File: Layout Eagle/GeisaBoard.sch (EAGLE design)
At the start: 20 parts, among them IC1 4052N, IC2 4052N, U1 328P

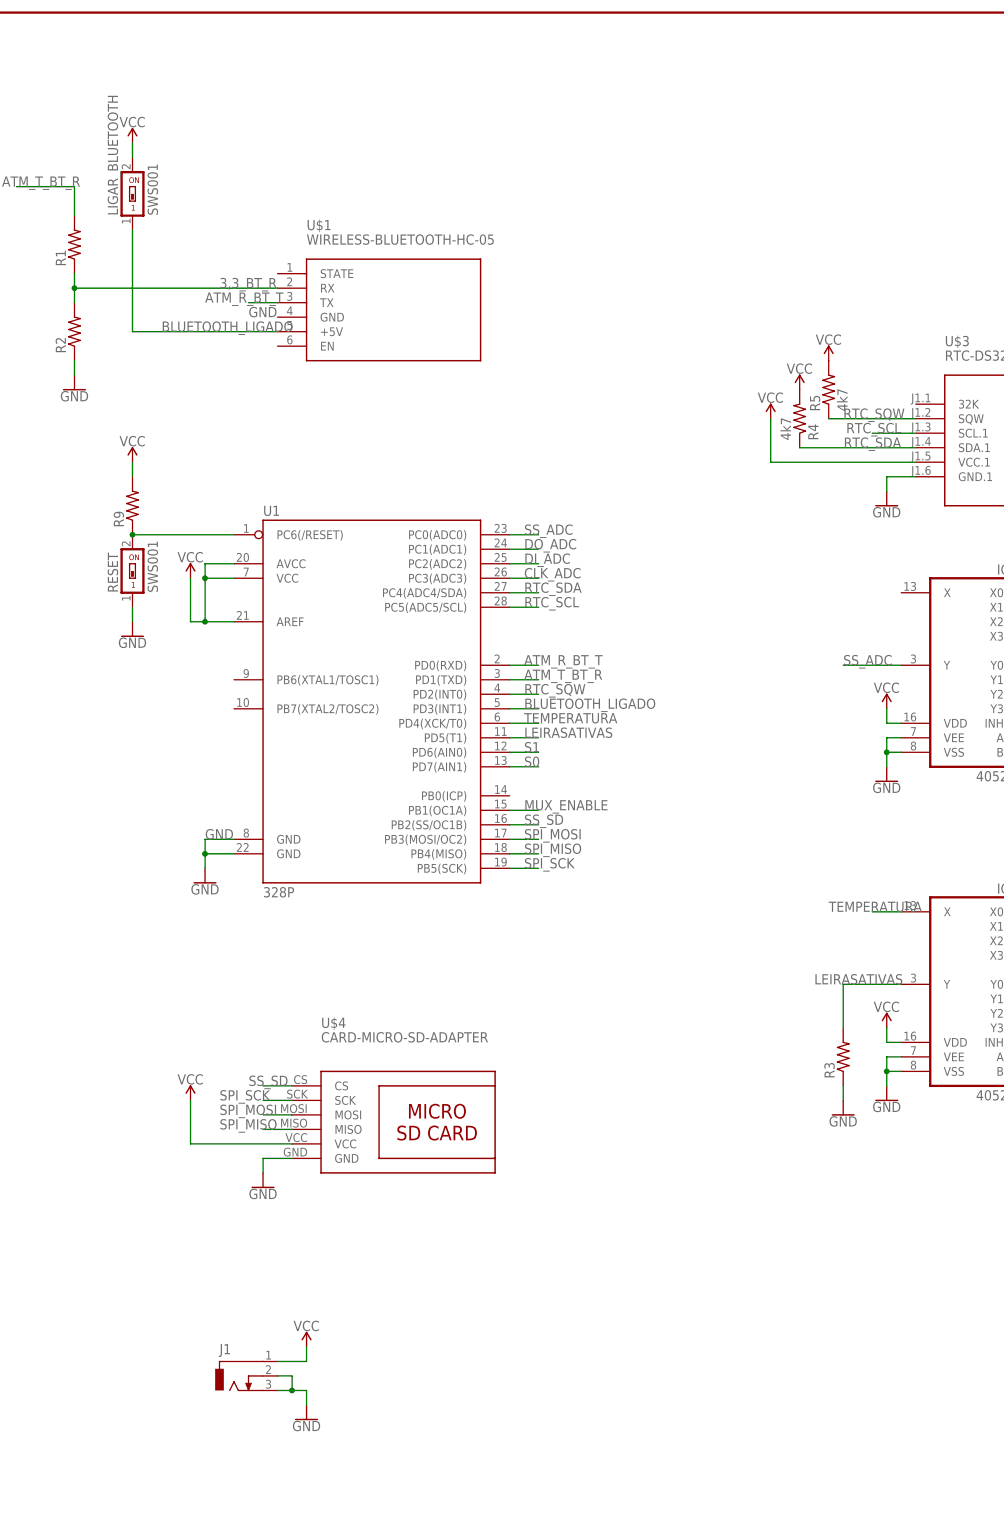
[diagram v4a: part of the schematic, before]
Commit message: Novo layout feito com melhores definições de espessura de trilhas e outros parâmetros
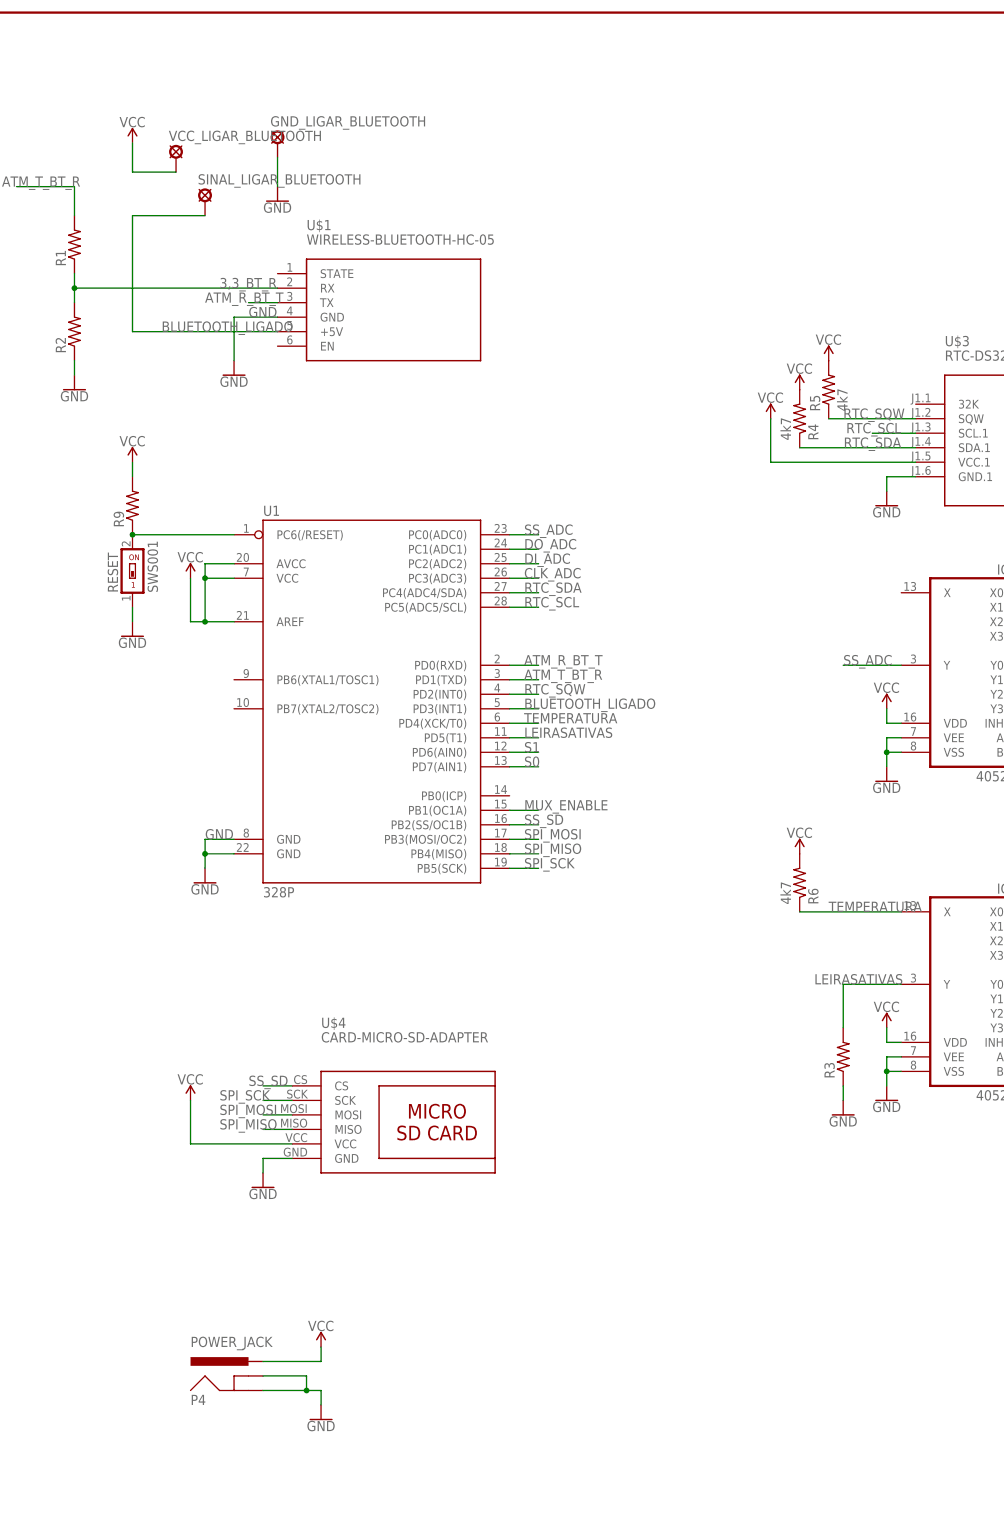
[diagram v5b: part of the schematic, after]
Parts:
- removed J1: (no value), con-jack:DCJ0303
- removed LIGAR_BLUETOOTH: SWS001, smd-special:SWS001
- added GND_LIGAR_BLUETOOTH, SINAL_LIGAR_BLUETOOTH, VCC_LIGAR_BLUETOOTH: LSP11, solpad:LSP11
- added P4: POWER_JACK, SparkFun-Connectors:POWER_JACK
- added R6: 4k7, rcl:R-US_0204/7
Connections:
- net BLUETOOTH_LIGADO: now also SINAL_LIGAR_BLUETOOTH.MP; no longer LIGAR_BLUETOOTH.1
- net GND: now also GND_LIGAR_BLUETOOTH.MP, P4.GND, P4.GNDBREAK, U$1.GND; no longer J1.2, J1.3
- net TEMPERATURA: now also R6.1
- net VCC: now also P4.PWR, R6.2, VCC_LIGAR_BLUETOOTH.MP; no longer J1.1, LIGAR_BLUETOOTH.2
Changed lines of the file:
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@@
 <?xml version="1.0" encoding="utf-8"?>
 <!DOCTYPE eagle SYSTEM "eagle.dtd">
-<eagle version="8.7.0">
+<eagle version="8.3.2">
 <drawing>
 <settings>
@@
 </variantdefs>
 <classes>
-<class number="0" name="default" width="0" drill="0">
+<class number="0" name="default" width="0.508" drill="0">
+</class>
+<class number="1" name="alimentação" width="1.016" drill="0">
 </class>
 </classes>
@@
 <part name="R9" library="rcl" library_urn="urn:adsk.eagle:library:334" deviceset="R-US_" device="0204/7" package3d_urn="urn:adsk.eagle:package:23498/1"/>
 <part name="RESET" library="smd-special" library_urn="urn:adsk.eagle:library:362" deviceset="SWS001" device="" package3d_urn="urn:adsk.eagle:package:26467/1"/>
-<part name="LIGAR_BLUETOOTH" library="smd-special" library_urn="urn:adsk.eagle:library:362" deviceset="SWS001" device="" package3d_urn="urn:adsk.eagle:package:26467/1"/>
 <part name="GND6" library="SparkFun-PowerSymbols" deviceset="GND" device=""/>
 <part name="GND7" library="SparkFun-PowerSymbols" deviceset="GND" device=""/>
@@
 <part name="SUPPLY8" library="SparkFun-PowerSymbols" deviceset="VCC" device=""/>
 <part name="SUPPLY9" library="SparkFun-PowerSymbols" deviceset="VCC" device=""/>
-<part name="J1" library="con-jack" library_urn="urn:adsk.eagle:library:154" deviceset="DCJ0303" device="" package3d_urn="urn:adsk.eagle:package:7493/1"/>
 <part name="GND11" library="SparkFun-PowerSymbols" deviceset="GND" device=""/>
 <part name="GND12" library="SparkFun-PowerSymbols" deviceset="GND" device=""/>
@@
 <part name="U$3" library="Geisa" deviceset="RTC-DS3231-AT24C32" device=""/>
 <part name="U$4" library="Geisa" deviceset="CARD-MICRO-SD-ADAPTER" device=""/>
+<part name="GND5" library="SparkFun-PowerSymbols" deviceset="GND" device=""/>
+<part name="R6" library="rcl" library_urn="urn:adsk.eagle:library:334" deviceset="R-US_" device="0204/7" package3d_urn="urn:adsk.eagle:package:23498/1" value="4k7"/>
+<part name="SUPPLY11" library="SparkFun-PowerSymbols" deviceset="VCC" device=""/>
+<part name="VCC_LIGAR_BLUETOOTH" library="solpad" library_urn="urn:adsk.eagle:library:364" deviceset="LSP11" device="" package3d_urn="urn:adsk.eagle:package:26502/1"/>
+<part name="SINAL_LIGAR_BLUETOOTH" library="solpad" library_urn="urn:adsk.eagle:library:364" deviceset="LSP11" device="" package3d_urn="urn:adsk.eagle:package:26502/1"/>
+<part name="GND_LIGAR_BLUETOOTH" library="solpad" library_urn="urn:adsk.eagle:library:364" deviceset="LSP11" device="" package3d_urn="urn:adsk.eagle:package:26502/1"/>
+<part name="GND10" library="SparkFun-PowerSymbols" deviceset="GND" device=""/>
+<part name="P4" library="SparkFun-Connectors" deviceset="POWER_JACK" device=""/>
 </parts>
 <sheets>
@@
 <instance part="R9" gate="G$1" x="-109.22" y="53.34" rot="R90"/>
 <instance part="RESET" gate="G$1" x="-109.22" y="40.64"/>
-<instance part="LIGAR_BLUETOOTH" gate="G$1" x="-109.22" y="106.68"/>
 <instance part="GND6" gate="1" x="149.86" y="81.28" rot="MR0"/>
 <instance part="GND7" gate="1" x="149.86" y="43.18" rot="MR0"/>
@@
 <instance part="SUPPLY8" gate="G$1" x="124.46" y="60.96"/>
 <instance part="SUPPLY9" gate="G$1" x="124.46" y="99.06"/>
-<instance part="J1" gate="G$1" x="-91.44" y="-99.06"/>
 <instance part="GND11" gate="1" x="15.24" y="-53.34"/>
 <instance part="GND12" gate="1" x="-86.36" y="-66.04"/>
@@
 <instance part="GND15" gate="1" x="-119.38" y="73.66"/>
 <instance part="GND16" gate="1" x="22.86" y="53.34"/>
-<instance part="GND17" gate="1" x="-78.74" y="-106.68"/>
+<instance part="GND17" gate="1" x="-76.2" y="-106.68"/>
 <instance part="SUPPLY4" gate="G$1" x="2.54" y="68.58"/>
 <instance part="SUPPLY5" gate="G$1" x="-99.06" y="-50.8"/>
@@
 <instance part="SUPPLY13" gate="G$1" x="-109.22" y="60.96"/>
 <instance part="SUPPLY14" gate="G$1" x="-109.22" y="116.84"/>
-<instance part="SUPPLY15" gate="G$1" x="-78.74" y="-93.98"/>
+<instance part="SUPPLY15" gate="G$1" x="-76.2" y="-93.98"/>
 <instance part="R4" gate="G$1" x="7.62" y="68.58" rot="MR90"/>
 <instance part="R5" gate="G$1" x="12.7" y="73.66" rot="R90"/>
@@
 <instance part="U$3" gate="G$1" x="45.72" y="66.04"/>
 <instance part="U$4" gate="G$1" x="-58.42" y="-58.42"/>
+<instance part="GND5" gate="1" x="-91.44" y="76.2"/>
+<instance part="R6" gate="G$1" x="7.62" y="-12.7" rot="MR90"/>
+<instance part="SUPPLY11" gate="G$1" x="7.62" y="-7.62" rot="MR0"/>
+<instance part="VCC_LIGAR_BLUETOOTH" gate="1" x="-101.6" y="114.3"/>
+<instance part="SINAL_LIGAR_BLUETOOTH" gate="1" x="-96.52" y="106.68"/>
+<instance part="GND_LIGAR_BLUETOOTH" gate="1" x="-83.82" y="116.84"/>
+<instance part="GND10" gate="1" x="-83.82" y="106.68"/>
+<instance part="P4" gate="G$1" x="-88.9" y="-104.14"/>
 </instances>
 <busses>
@@
 </segment>
 </net>
-<net name="GND" class="0">
+<net name="GND" class="1">
 <segment>
 <wire x1="-96.52" y1="-10.16" x2="-96.52" y2="-7.62" width="0.1524" layer="91"/>
@@
 </segment>
 <segment>
-<pinref part="J1" gate="G$1" pin="3"/>
 <pinref part="GND17" gate="1" pin="GND"/>
-<wire x1="-83.82" y1="-101.6" x2="-81.28" y2="-101.6" width="0.1524" layer="91"/>
-<wire x1="-81.28" y1="-101.6" x2="-78.74" y2="-101.6" width="0.1524" layer="91"/>
-<wire x1="-78.74" y1="-101.6" x2="-78.74" y2="-104.14" width="0.1524" layer="91"/>
-<pinref part="J1" gate="G$1" pin="2"/>
-<wire x1="-83.82" y1="-99.06" x2="-81.28" y2="-99.06" width="0.1524" layer="91"/>
-<wire x1="-81.28" y1="-99.06" x2="-81.28" y2="-101.6" width="0.1524" layer="91"/>
-<junction x="-81.28" y="-101.6"/>
+<wire x1="-86.36" y1="-101.6" x2="-78.74" y2="-101.6" width="0.1524" layer="91"/>
+<wire x1="-78.74" y1="-101.6" x2="-76.2" y2="-101.6" width="0.1524" layer="91"/>
+<wire x1="-76.2" y1="-101.6" x2="-76.2" y2="-104.14" width="0.1524" layer="91"/>
+<wire x1="-86.36" y1="-99.06" x2="-78.74" y2="-99.06" width="0.1524" layer="91"/>
+<wire x1="-78.74" y1="-99.06" x2="-78.74" y2="-101.6" width="0.1524" layer="91"/>
+<junction x="-78.74" y="-101.6"/>
+<pinref part="P4" gate="G$1" pin="GND"/>
+<pinref part="P4" gate="G$1" pin="GNDBREAK"/>
 </segment>
 <segment>
@@
 <wire x1="22.86" y1="58.42" x2="22.86" y2="55.88" width="0.1524" layer="91"/>
 </segment>
+<segment>
+<pinref part="GND10" gate="1" pin="GND"/>
+<pinref part="GND_LIGAR_BLUETOOTH" gate="1" pin="MP"/>
+<wire x1="-83.82" y1="109.22" x2="-83.82" y2="114.3" width="0.1524" layer="91"/>
+</segment>
+<segment>
+<pinref part="U$1" gate="G$1" pin="GND"/>
+<pinref part="GND5" gate="1" pin="GND"/>
+<wire x1="-83.82" y1="86.36" x2="-91.44" y2="86.36" width="0.1524" layer="91"/>
+<wire x1="-91.44" y1="86.36" x2="-91.44" y2="78.74" width="0.1524" layer="91"/>
+</segment>
 </net>
 <net name="N$12" class="0">
@@
 <net name="TEMPERATURA" class="0">
 <segment>
-<wire x1="25.4" y1="-17.78" x2="20.32" y2="-17.78" width="0.1524" layer="91"/>
 <label x="12.7" y="-17.78" size="1.778" layer="95"/>
 <pinref part="IC2" gate="A" pin="X"/>
+<pinref part="R6" gate="G$1" pin="1"/>
+<wire x1="25.4" y1="-17.78" x2="7.62" y2="-17.78" width="0.1524" layer="91"/>
 </segment>
 <segment>
@@
 </segment>
 </net>
-<net name="VCC" class="0">
+<net name="VCC" class="1">
 <segment>
 <wire x1="124.46" y1="-25.4" x2="129.54" y2="-25.4" width="0.1524" layer="91"/>
@@
 </segment>
 <segment>
-<pinref part="J1" gate="G$1" pin="1"/>
 <pinref part="SUPPLY15" gate="G$1" pin="VCC"/>
-<wire x1="-83.82" y1="-96.52" x2="-78.74" y2="-96.52" width="0.1524" layer="91"/>
-<wire x1="-78.74" y1="-96.52" x2="-78.74" y2="-93.98" width="0.1524" layer="91"/>
+<wire x1="-86.36" y1="-96.52" x2="-76.2" y2="-96.52" width="0.1524" layer="91"/>
+<wire x1="-76.2" y1="-96.52" x2="-76.2" y2="-93.98" width="0.1524" layer="91"/>
+<pinref part="P4" gate="G$1" pin="PWR"/>
 </segment>
 <segment>
@@
 </segment>
 <segment>
-<pinref part="LIGAR_BLUETOOTH" gate="G$1" pin="2"/>
 <pinref part="SUPPLY14" gate="G$1" pin="VCC"/>
-<wire x1="-109.22" y1="116.84" x2="-109.22" y2="114.3" width="0.1524" layer="91"/>
+<pinref part="VCC_LIGAR_BLUETOOTH" gate="1" pin="MP"/>
+<wire x1="-101.6" y1="111.76" x2="-109.22" y2="111.76" width="0.1524" layer="91"/>
+<wire x1="-109.22" y1="111.76" x2="-109.22" y2="116.84" width="0.1524" layer="91"/>
 </segment>
 <segment>
@@
 <pinref part="IC2" gate="A" pin="VDD"/>
 </segment>
+<segment>
+<pinref part="R6" gate="G$1" pin="2"/>
+<pinref part="SUPPLY11" gate="G$1" pin="VCC"/>
+</segment>
 </net>
 <net name="BLUETOOTH_LIGADO" class="0">
@@
 </segment>
 <segment>
-<pinref part="LIGAR_BLUETOOTH" gate="G$1" pin="1"/>
-<wire x1="-109.22" y1="101.6" x2="-109.22" y2="83.82" width="0.1524" layer="91"/>
+<wire x1="-109.22" y1="104.14" x2="-109.22" y2="83.82" width="0.1524" layer="91"/>
 <pinref part="U$1" gate="G$1" pin="+5V"/>
 <wire x1="-109.22" y1="83.82" x2="-83.82" y2="83.82" width="0.1524" layer="91"/>
 <label x="-104.14" y="83.82" size="1.778" layer="95"/>
+<pinref part="SINAL_LIGAR_BLUETOOTH" gate="1" pin="MP"/>
+<wire x1="-96.52" y1="104.14" x2="-109.22" y2="104.14" width="0.1524" layer="91"/>
 </segment>
 </net>
@@
 </sheet>
 </sheets>
+<errors>
+</errors>
 </schematic>
 </drawing>

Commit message: Layout
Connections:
- net N$12 renamed RESET/
- net GND: now also SAIDA_L0.5, SAIDA_L1.5, SAIDA_L2.5, SAIDA_L3.5; no longer SAIDA_L0.9, SAIDA_L1.9, SAIDA_L2.9, SAIDA_L3.9
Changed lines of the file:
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@@
 <instance part="R9" gate="G$1" x="-109.22" y="53.34" rot="R90"/>
 <instance part="RESET" gate="G$1" x="-109.22" y="40.64"/>
-<instance part="GND6" gate="1" x="149.86" y="81.28" rot="MR0"/>
-<instance part="GND7" gate="1" x="149.86" y="43.18" rot="MR0"/>
-<instance part="GND8" gate="1" x="149.86" y="0" rot="MR0"/>
-<instance part="GND9" gate="1" x="149.86" y="-40.64" rot="MR0"/>
+<instance part="GND6" gate="1" x="127" y="81.28" rot="MR0"/>
+<instance part="GND7" gate="1" x="127" y="43.18" rot="MR0"/>
+<instance part="GND8" gate="1" x="127" y="0" rot="MR0"/>
+<instance part="GND9" gate="1" x="127" y="-40.64" rot="MR0"/>
 <instance part="SUPPLY6" gate="G$1" x="124.46" y="-22.86"/>
 <instance part="SUPPLY7" gate="G$1" x="124.46" y="17.78"/>
@@
 </segment>
 <segment>
-<wire x1="144.78" y1="86.36" x2="149.86" y2="86.36" width="0.1524" layer="91"/>
 <pinref part="GND6" gate="1" pin="GND"/>
-<wire x1="149.86" y1="86.36" x2="149.86" y2="83.82" width="0.1524" layer="91"/>
-<pinref part="SAIDA_L0" gate="G$1" pin="9"/>
-</segment>
-<segment>
-<wire x1="144.78" y1="48.26" x2="149.86" y2="48.26" width="0.1524" layer="91"/>
+<wire x1="127" y1="86.36" x2="127" y2="83.82" width="0.1524" layer="91"/>
+<pinref part="SAIDA_L0" gate="G$1" pin="5"/>
+<wire x1="129.54" y1="86.36" x2="127" y2="86.36" width="0.1524" layer="91"/>
+</segment>
+<segment>
 <pinref part="GND7" gate="1" pin="GND"/>
-<wire x1="149.86" y1="45.72" x2="149.86" y2="48.26" width="0.1524" layer="91"/>
-<pinref part="SAIDA_L1" gate="G$1" pin="9"/>
-</segment>
-<segment>
-<wire x1="149.86" y1="5.08" x2="144.78" y2="5.08" width="0.1524" layer="91"/>
+<wire x1="127" y1="45.72" x2="127" y2="48.26" width="0.1524" layer="91"/>
+<pinref part="SAIDA_L1" gate="G$1" pin="5"/>
+<wire x1="129.54" y1="48.26" x2="127" y2="48.26" width="0.1524" layer="91"/>
+</segment>
+<segment>
 <pinref part="GND8" gate="1" pin="GND"/>
-<wire x1="149.86" y1="2.54" x2="149.86" y2="5.08" width="0.1524" layer="91"/>
-<pinref part="SAIDA_L2" gate="G$1" pin="9"/>
-</segment>
-<segment>
-<wire x1="149.86" y1="-35.56" x2="144.78" y2="-35.56" width="0.1524" layer="91"/>
+<wire x1="127" y1="2.54" x2="127" y2="5.08" width="0.1524" layer="91"/>
+<pinref part="SAIDA_L2" gate="G$1" pin="5"/>
+<wire x1="129.54" y1="5.08" x2="127" y2="5.08" width="0.1524" layer="91"/>
+</segment>
+<segment>
 <pinref part="GND9" gate="1" pin="GND"/>
-<wire x1="149.86" y1="-38.1" x2="149.86" y2="-35.56" width="0.1524" layer="91"/>
-<pinref part="SAIDA_L3" gate="G$1" pin="9"/>
+<wire x1="127" y1="-38.1" x2="127" y2="-35.56" width="0.1524" layer="91"/>
+<pinref part="SAIDA_L3" gate="G$1" pin="5"/>
+<wire x1="129.54" y1="-35.56" x2="127" y2="-35.56" width="0.1524" layer="91"/>
 </segment>
 <segment>
@@
 </segment>
 </net>
-<net name="N$12" class="0">
+<net name="RESET/" class="0">
 <segment>
 <pinref part="RESET" gate="G$1" pin="2"/>
@@
 <wire x1="-91.44" y1="48.26" x2="-109.22" y2="48.26" width="0.1524" layer="91"/>
 <junction x="-109.22" y="48.26"/>
-</segment>
-</net>
+<label x="-96.52" y="48.26" size="1.778" layer="95"/>
+</segment>
+</net>
